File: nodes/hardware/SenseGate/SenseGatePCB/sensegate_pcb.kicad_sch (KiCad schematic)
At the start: 41 parts, among them J10 Conn_01x02_Pin, J3 Conn_01x02_Socket, J4 Conn_01x24_Pin, J5 Conn_01x04_Socket, J6 Conn_01x04_Socket, J7 Conn_01x04_Socket, J8 Conn_01x04_Socket, J9 Conn_01x04_Socket, Q4 SS8050, SW1 SW_Reed, SW2 SW_Reed, SW3 SW_Reed, SW5 SW_DPDT_x2, U1 DD05CVSA, U2 mt3608_dcdc_converter

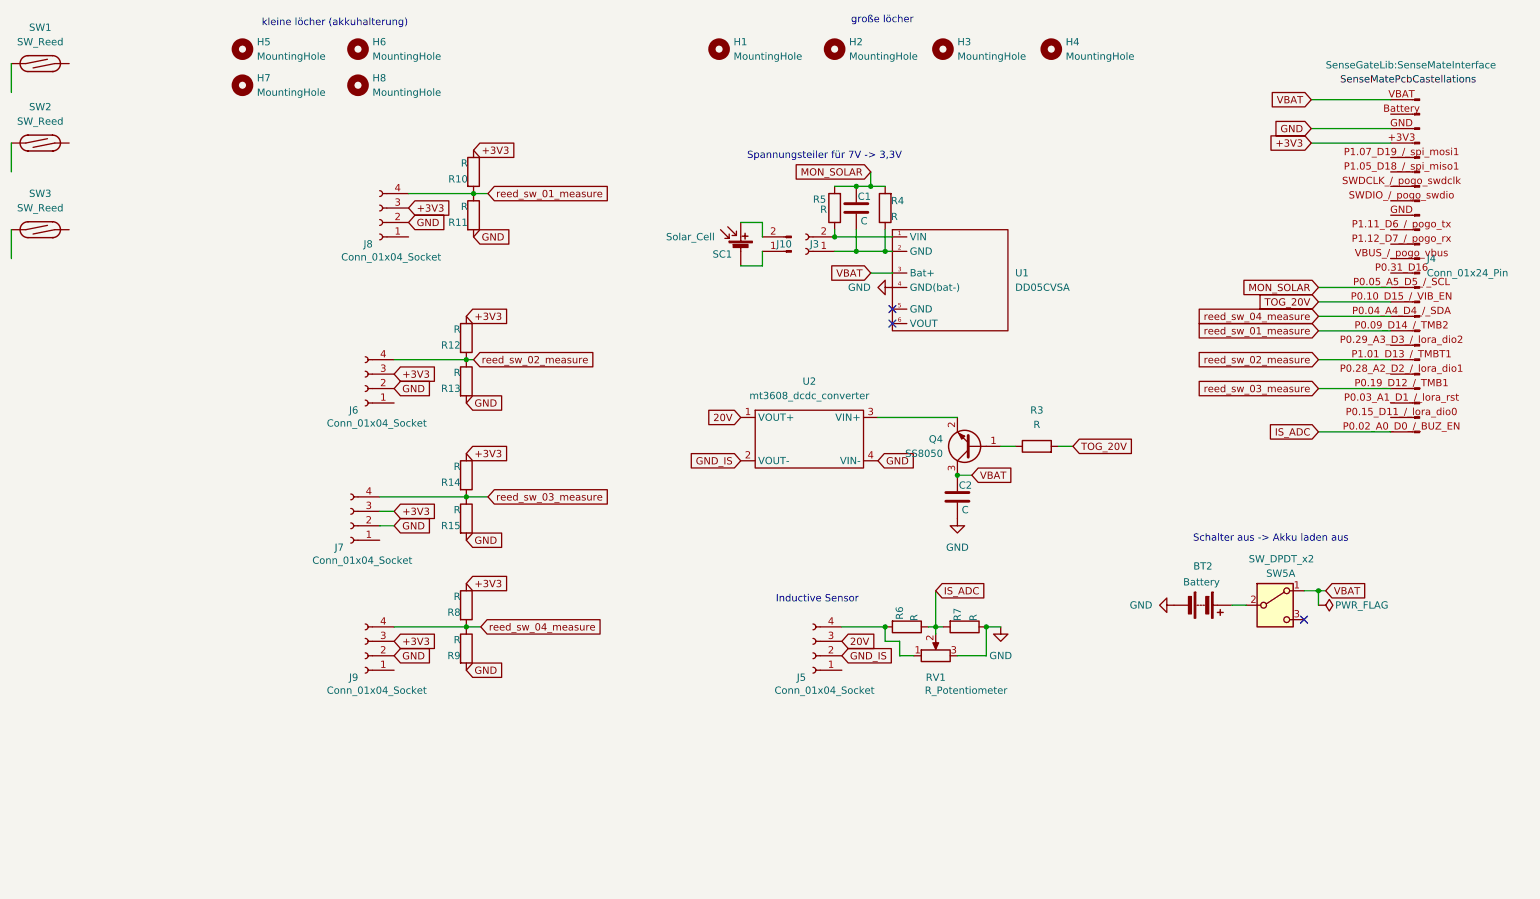
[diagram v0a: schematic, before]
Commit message: implemented michels complaints, todo: rulechecker and gen gerber files
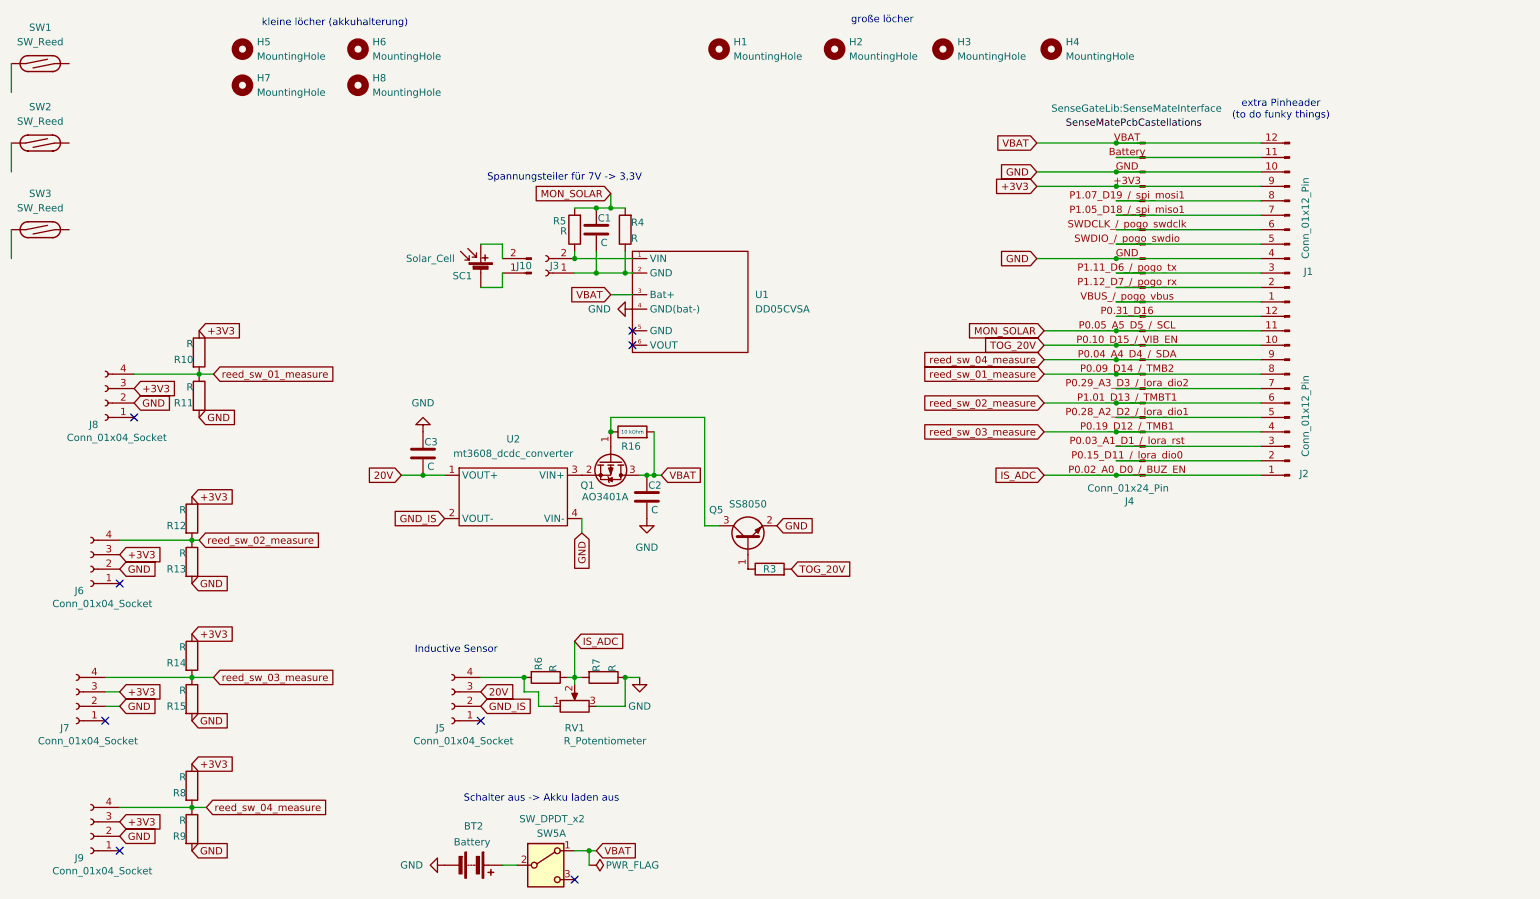
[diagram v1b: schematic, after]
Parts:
- removed Q4: SS8050, Package_TO_SOT_SMD:SOT-23, symbol Transistor_BJT:SS8050
- added C3: C, Capacitor_SMD:C_0805_2012Metric_Pad1.18x1.45mm_HandSolder, symbol Device:C
- added J1, J2: Conn_01x12_Pin, Connector_PinHeader_2.54mm:PinHeader_1x12_P2.54mm_Vertical, symbol Connector:Conn_01x12_Pin
- added Q1: AO3401A, Package_TO_SOT_SMD:SOT-23, symbol Transistor_FET:AO3401A
- added Q5: SS8050, Package_TO_SOT_SMD:SOT-23, symbol Transistor_BJT:SS8050
- added R16: R, Resistor_SMD:R_0805_2012Metric, symbol Device:R
- C1, C2: footprint Capacitor_SMD:C_0805_2012Metric -> Capacitor_SMD:C_0805_2012Metric_Pad1.18x1.45mm_HandSolder
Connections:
- net +3V3: now also J1.9 (Pin_9)
- net 20V: now also C3.2
- net GND: now also C3.1, J1.10 (Pin_10), J1.4 (Pin_4), Q5.2 (E)
- net IS_ADC: now also J2.1 (Pin_1)
- net MON_SOLAR: now also J2.11 (Pin_11)
- net TOG_20V: now also J2.10 (Pin_10)
- net VBAT: now also J1.12 (Pin_12), Q1.3 (D), R16.2
- net reed_sw_01_measure: now also J2.8 (Pin_8)
- net reed_sw_02_measure: now also J2.6 (Pin_6)
- net reed_sw_03_measure: now also J2.4 (Pin_4)
- net reed_sw_04_measure: now also J2.9 (Pin_9)
- net at R3.1: now also Q5.1 (B)
- net at U2.3 (VIN+): now also Q1.2 (S)
- net at J4.Battery (Pin_23): now also J1.11 (Pin_11)
- net at J4.P0.03_A1_D1_/_lora_rst (Pin_3): now also J2.3 (Pin_3)
- net at J4.P0.15_D11_/_lora_dio0 (Pin_2): now also J2.2 (Pin_2)
- net at J4.P0.28_A2_D2_/_lora_dio1 (Pin_5): now also J2.5 (Pin_5)
- net at J4.P0.29_A3_D3_/_lora_dio2 (Pin_7): now also J2.7 (Pin_7)
- net at J4.P0.31_D16 (Pin_12): now also J2.12 (Pin_12)
- net at J4.P1.05_D18_/_spi_miso1 (Pin_19): now also J1.7 (Pin_7)
- net at J4.P1.07_D19_/_spi_mosi1 (Pin_20): now also J1.8 (Pin_8)
- net at J4.P1.11_D6_/_pogo_tx (Pin_15): now also J1.3 (Pin_3)
- net at J4.P1.12_D7_/_pogo_rx (Pin_14): now also J1.2 (Pin_2)
- net at J4.SWDCLK_/_pogo_swdclk (Pin_18): now also J1.6 (Pin_6)
- net at J4.SWDIO_/_pogo_swdio (Pin_17): now also J1.5 (Pin_5)
- net at J4.VBUS_/_pogo_vbus (Pin_13): now also J1.1 (Pin_1)
- new net: Q1.1 (G), Q5.3 (C), R16.1
- no-connect marks 3 -> 8
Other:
- note added: "10 kOhm"
- note added: "extra Pinheader (to do funky things)"
- moved on the sheet: BT2, C1, C2, J10, J3, J4, J5, J6, J7, J8, J9, R10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

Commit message: figuring out mosfet useage
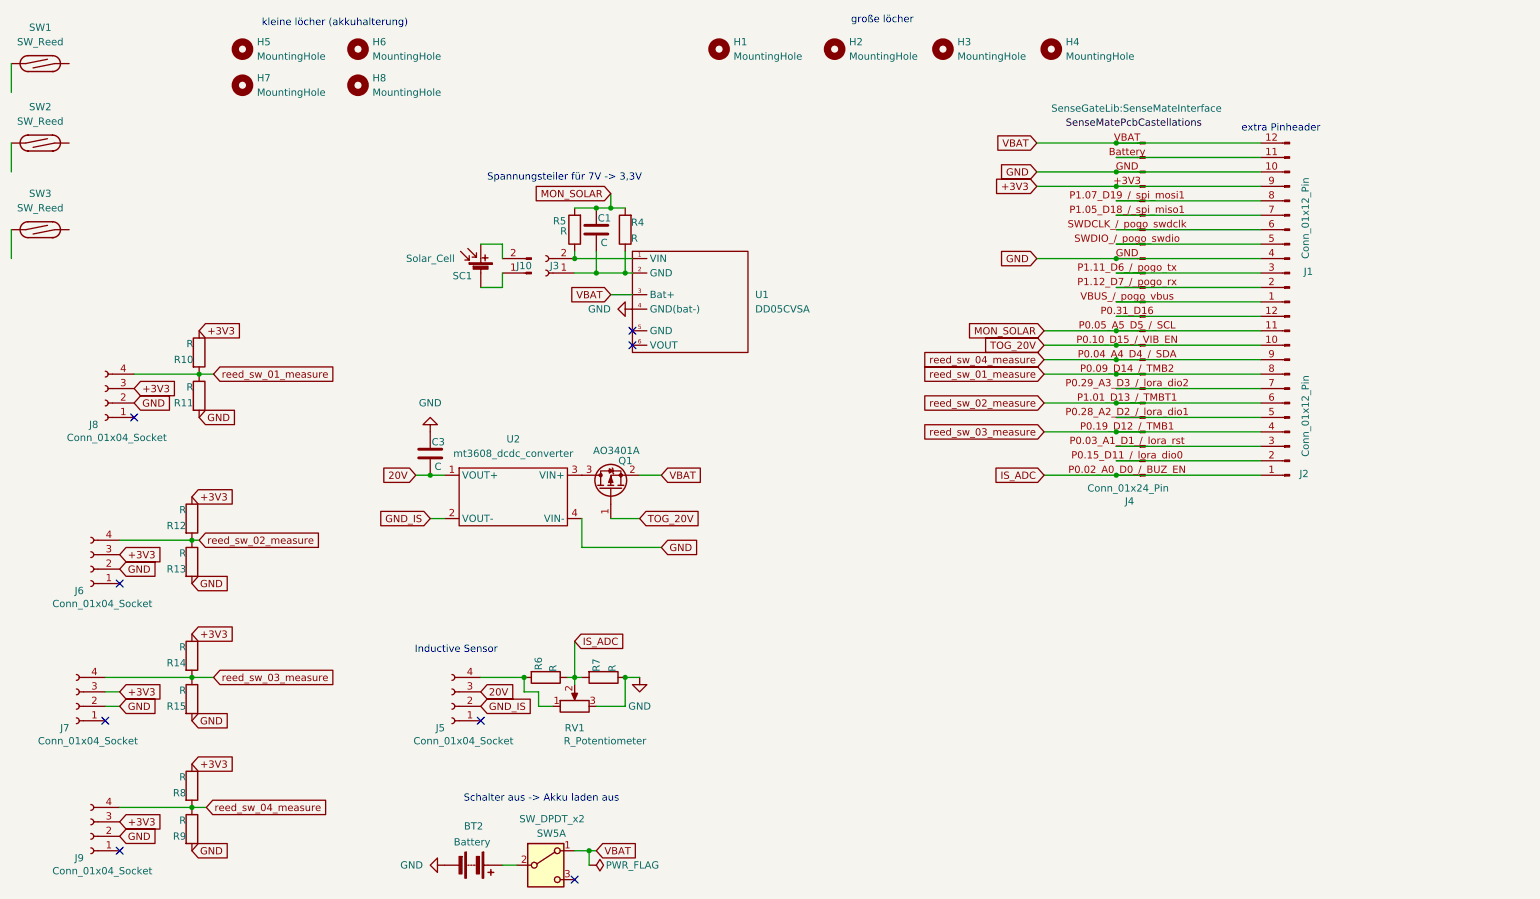
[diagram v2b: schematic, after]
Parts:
- removed C2: C, Capacitor_SMD:C_0805_2012Metric_Pad1.18x1.45mm_HandSolder, symbol Device:C
- removed Q5: SS8050, Package_TO_SOT_SMD:SOT-23, symbol Transistor_BJT:SS8050
- removed R16, R3: R, Resistor_SMD:R_0805_2012Metric, symbol Device:R
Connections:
- net TOG_20V: now also Q1.1 (G)
- net VBAT: now also Q1.2 (S); no longer Q1.3 (D)
- net at U2.3 (VIN+): now also Q1.3 (D); no longer Q1.2 (S)
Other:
- note added: "extra Pinheader"
- note removed: "10 kOhm"
- note removed: "extra Pinheader (to do funky things)"
- moved on the sheet: C3, Q1

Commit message: added description for resistor values
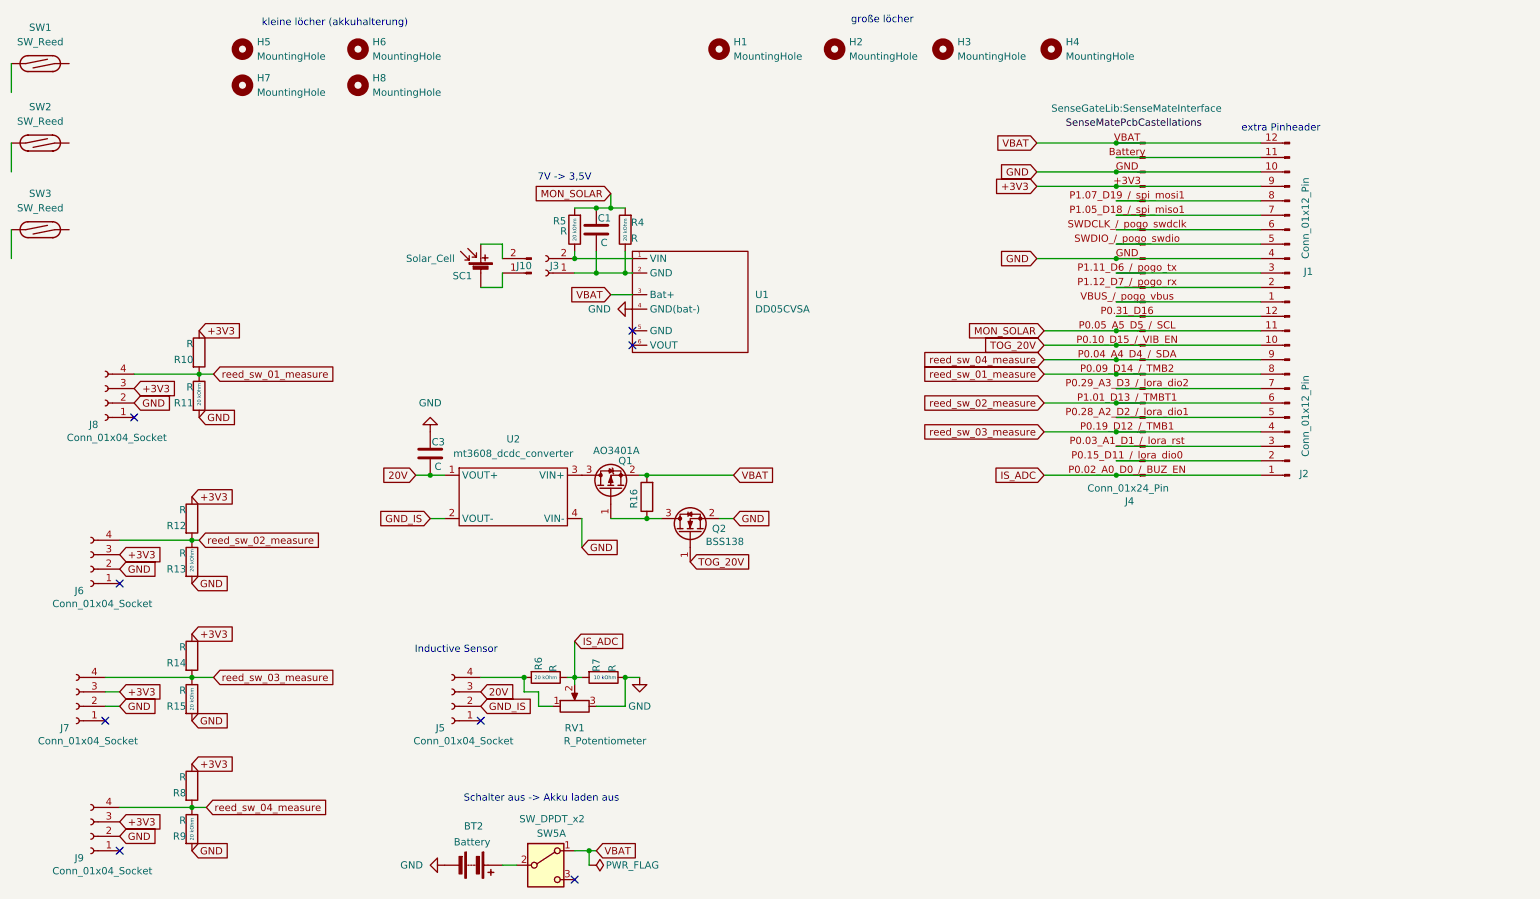
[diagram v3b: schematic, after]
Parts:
- added Q2: BSS138, Package_TO_SOT_SMD:SOT-23, symbol Transistor_FET:BSS138
- added R16: R, Resistor_SMD:R_0805_2012Metric, symbol Device:R
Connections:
- net GND: now also Q2.2 (S)
- net TOG_20V: now also Q2.1 (G); no longer Q1.1 (G)
- net VBAT: now also R16.2
- new net: Q1.1 (G), Q2.3 (D), R16.1
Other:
- note added: "10 kOhm"
- note added: "20 kOhm"
- note added: "7V -> 3,5V"
- note removed: "Spannungsteiler für 7V -> 3,3V"

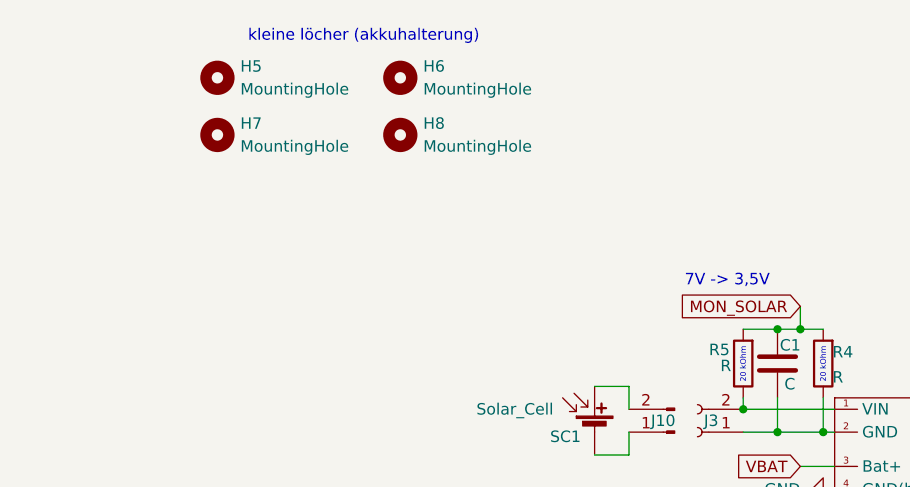
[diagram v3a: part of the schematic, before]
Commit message: added hole to access mate reset pin, optimized power swtich placement and generated new gerber files
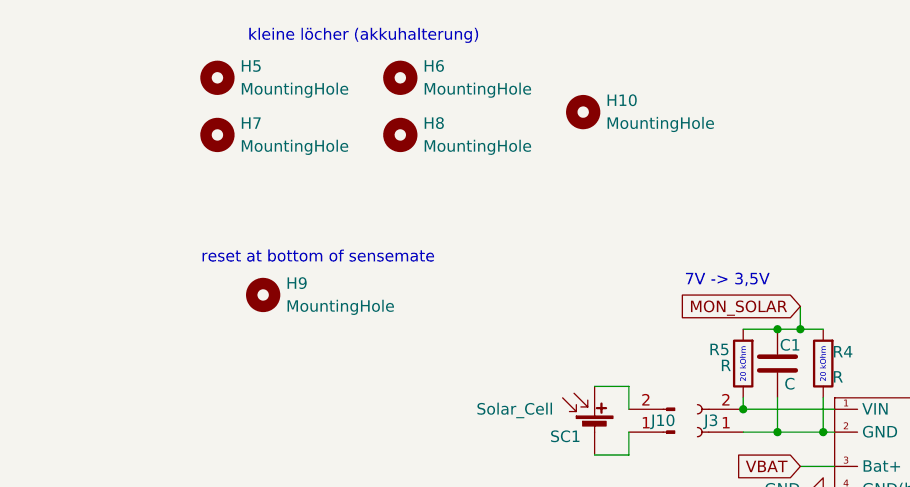
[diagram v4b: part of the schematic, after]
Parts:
- added H10: MountingHole, MountingHole:MountingHole_2.2mm_M2, symbol Mechanical:MountingHole
- added H9: MountingHole, MountingHole:MountingHole_4mm, symbol Mechanical:MountingHole
- BT2: footprint Connector_JST:JST_PH_S2B-PH-K_1x02_P2.00mm_Horizontal -> Connector_JST:JST_PH_B2B-PH-K_1x02_P2.00mm_Vertical
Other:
- note added: "reset at bottom of sensemate"
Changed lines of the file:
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@@
 		)
 	)
+	(text "reset at bottom of sensemate"
+		(exclude_from_sim no)
+		(at 70.866 41.656 0)
+		(effects
+			(font
+				(size 1.27 1.27)
+			)
+		)
+	)
 	(text "20 kOhm"
 		(exclude_from_sim no)
@@
 			)
 		)
-		(property "Footprint" "Connector_JST:JST_PH_S2B-PH-K_1x02_P2.00mm_Horizontal"
+		(property "Footprint" "Connector_JST:JST_PH_B2B-PH-K_1x02_P2.00mm_Vertical"
 			(at 101.854 165.1 90)
 			(hide yes)
@@
 	)
 	(symbol
+		(lib_id "Mechanical:MountingHole")
+		(at 64.77 45.72 0)
+		(unit 1)
+		(body_style 1)
+		(exclude_from_sim no)
+		(in_bom no)
+		(on_board yes)
+		(in_pos_files yes)
+		(dnp no)
+		(fields_autoplaced yes)
+		(property "Reference" "H9"
+			(at 67.31 44.4499 0)
+			(show_name no)
+			(do_not_autoplace no)
+			(effects
+				(font
+					(size 1.27 1.27)
+				)
+				(justify left)
+			)
+		)
+		(property "Value" "MountingHole"
+			(at 67.31 46.9899 0)
+			(show_name no)
+			(do_not_autoplace no)
+			(effects
+				(font
+					(size 1.27 1.27)
+				)
+				(justify left)
+			)
+		)
+		(property "Footprint" "MountingHole:MountingHole_4mm"
+			(at 64.77 45.72 0)
+			(hide yes)
+			(show_name no)
+			(do_not_autoplace no)
+			(effects
+				(font
+					(size 1.27 1.27)
+				)
+			)
+		)
+		(property "Datasheet" ""
+			(at 64.77 45.72 0)
+			(hide yes)
+			(show_name no)
+			(do_not_autoplace no)
+			(effects
+				(font
+					(size 1.27 1.27)
+				)
+			)
+		)
+		(property "Description" "Mounting Hole without connection"
+			(at 64.77 45.72 0)
+			(hide yes)
+			(show_name no)
+			(do_not_autoplace no)
+			(effects
+				(font
+					(size 1.27 1.27)
+				)
+			)
+		)
+		(instances
+			(project "sensegate_pcb"
+				(path "/cab49cbb-a41f-4356-a83b-79a7aa8374de"
+					(reference "H9")
+					(unit 1)
+				)
+			)
+		)
+	)
+	(symbol
 		(lib_id "Device:C")
 		(at 121.92 53.34 0)
@@
 					(unit 1)
 				)
+			)
+		)
+	)
+	(symbol
+		(lib_id "Mechanical:MountingHole")
+		(at 100.33 25.4 0)
+		(unit 1)
+		(body_style 1)
+		(exclude_from_sim no)
+		(in_bom no)
+		(on_board yes)
+		(in_pos_files yes)
+		(dnp no)
+		(fields_autoplaced yes)
+		(property "Reference" "H10"
+			(at 102.87 24.1299 0)
+			(show_name no)
+			(do_not_autoplace no)
+			(effects
+				(font
+					(size 1.27 1.27)
+				)
+				(justify left)
+			)
+		)
+		(property "Value" "MountingHole"
+			(at 102.87 26.6699 0)
+			(show_name no)
+			(do_not_autoplace no)
+			(effects
+				(font
+					(size 1.27 1.27)
+				)
+				(justify left)
+			)
+		)
+		(property "Footprint" "MountingHole:MountingHole_2.2mm_M2"
+			(at 100.33 25.4 0)
+			(hide yes)
+			(show_name no)
+			(do_not_autoplace no)
+			(effects
+				(font
+					(size 1.27 1.27)
+				)
+			)
+		)
+		(property "Datasheet" ""
+			(at 100.33 25.4 0)
+			(hide yes)
+			(show_name no)
+			(do_not_autoplace no)
+			(effects
+				(font
+					(size 1.27 1.27)
+				)
+			)
+		)
+		(property "Description" "Mounting Hole without connection"
+			(at 100.33 25.4 0)
+			(hide yes)
+			(show_name no)
+			(do_not_autoplace no)
+			(effects
+				(font
+					(size 1.27 1.27)
+				)
+			)
+		)
+		(instances
+			(project "sensegate_pcb"
+				(path "/cab49cbb-a41f-4356-a83b-79a7aa8374de"
+					(reference "H10")
+					(unit 1)
+				)
